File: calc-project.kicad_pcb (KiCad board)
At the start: 2 copper layers, 100 x 100 mm, 39 parts, among them J1 PinSocket_1x20_Right, J2 PinSocket_1x20_Left, J3 Conn_01x14, SW1 SW_Push_45deg, SW10 SW_Push_45deg, SW11 SW_Push_45deg, SW12 SW_Push_45deg, SW13 SW_Push_45deg, SW14 SW_Push_45deg, SW15 SW_Push_45deg, SW16 SW_Push_45deg, SW17 SW_Push_45deg, SW18 SW_Push_45deg, SW19 SW_Push_45deg, SW2 SW_Push_45deg, SW20 SW_Push_45deg, SW21 SW_Push_45deg, SW22 SW_Push_45deg, SW23 SW_Push_45deg, SW24 SW_Push_45deg, SW25 SW_Push_45deg, SW26 SW_Push_45deg, SW27 SW_Push_45deg, SW28 SW_Push_45deg, SW29 SW_Push_45deg, SW3 SW_Push_45deg, SW30 SW_Push_45deg, SW31 SW_Push_45deg, SW32 SW_Push_45deg, SW33 SW_Push_45deg, SW34 SW_Push_45deg, SW35 SW_Push_45deg, SW36 SW_Push_45deg, SW4 SW_Push_45deg, SW5 SW_Push_45deg, SW6 SW_Push_45deg, SW7 SW_Push_45deg, SW8 SW_Push_45deg, SW9 SW_Push_45deg

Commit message: random stuff, i think it helps
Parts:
- added H1: MountingHole, MountingHole:MountingHole_2.1mm, F.Cu at (35.0, 93.0)
- added H2: MountingHole, MountingHole:MountingHole_2.1mm, F.Cu at (124.0, 93.0)
- added H3: MountingHole, MountingHole:MountingHole_2.1mm, F.Cu at (35.0, 187.0)
- added H4: MountingHole, MountingHole:MountingHole_2.1mm, F.Cu at (124.0, 187.0)
- added H5: MountingHole, MountingHole:MountingHole_2.1mm, F.Cu at (49.0, 120.0)
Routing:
- net +3.3V: track 58.1 -> 60.8 mm
- net col 1: track 133.8 -> 131.4 mm
- net row 3: track 131.3 -> 129.7 mm
- net col 0: track 116.0 -> 114.4 mm
- net row 5: track 151.0 -> 149.9 mm
- net col 4: track 174.4 -> 174.7 mm, vias 2 -> 0

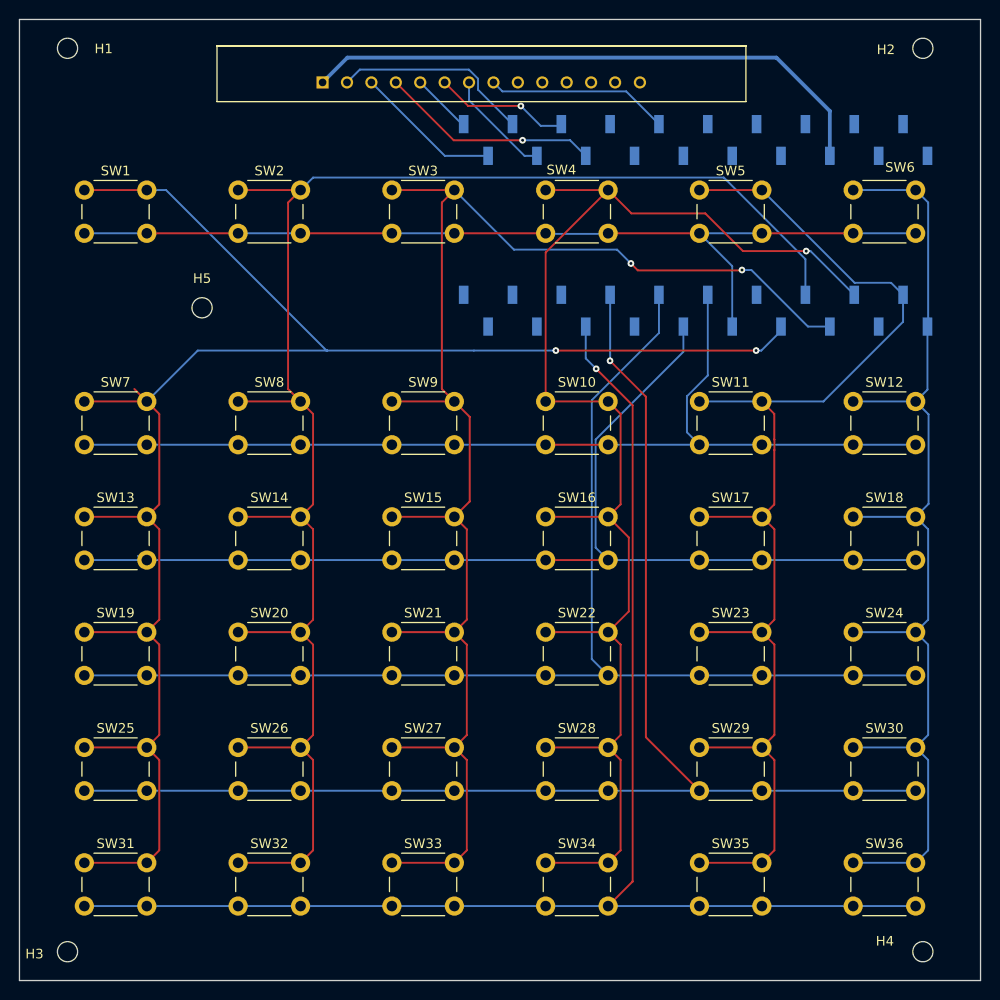
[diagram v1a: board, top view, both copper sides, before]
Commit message: better dimensions
Didn't have to be so wide, so I put all the components closer together and rerouted the whole thing
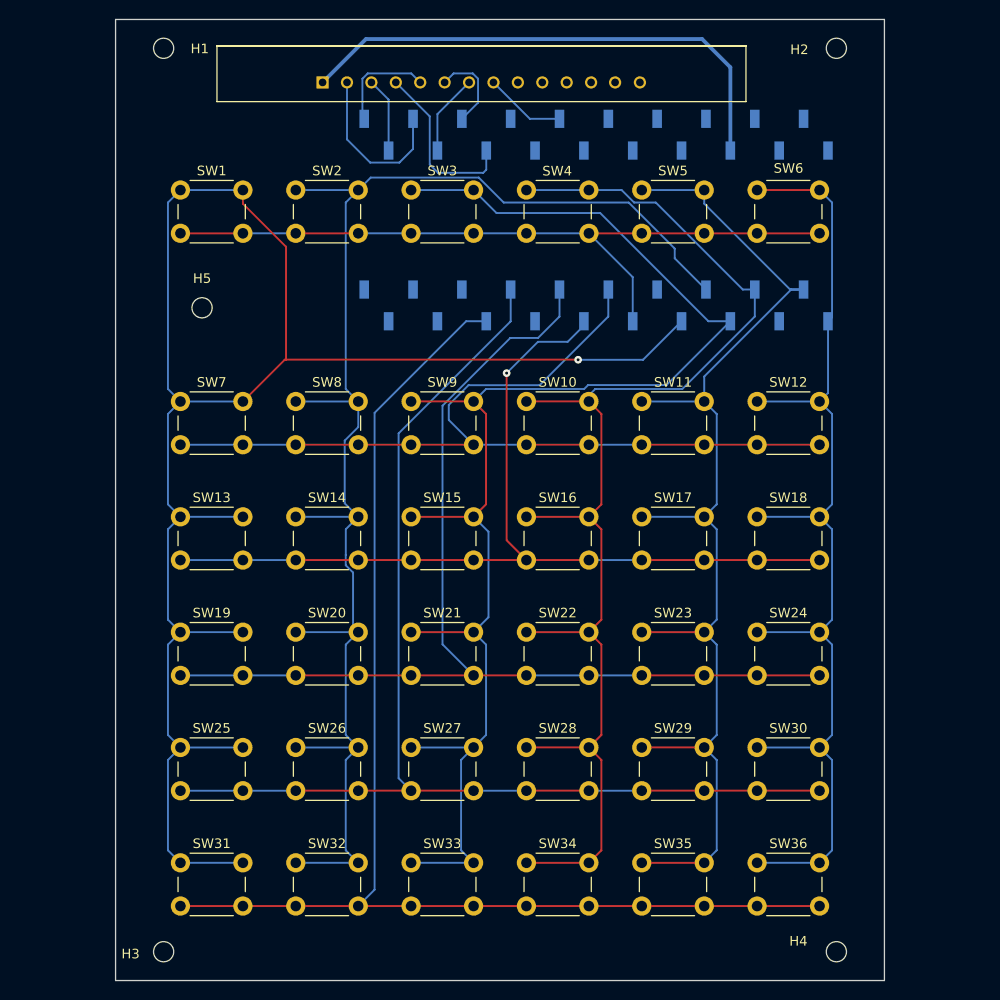
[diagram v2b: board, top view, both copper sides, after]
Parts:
- moved J1 10.4 mm to (90.0, 102.0)
- moved J2 10.4 mm to (90.0, 119.8)
- moved H1 10.0 mm to (45.0, 93.0)
- moved H3 10.0 mm to (45.0, 187.0)
- moved SW1 10.0 mm to (50.0, 110.0)
- moved SW12 10.0 mm to (110.0, 132.0)
- moved SW13 10.0 mm to (50.0, 144.0)
- moved SW18 10.0 mm to (110.0, 144.0)
- moved SW19 10.0 mm to (50.0, 156.0)
- moved SW24 10.0 mm to (110.0, 156.0)
- moved SW25 10.0 mm to (50.0, 168.0)
- moved SW30 10.0 mm to (110.0, 168.0)
- moved SW31 10.0 mm to (50.0, 180.0)
- moved SW36 10.0 mm to (110.0, 180.0)
- moved SW6 10.0 mm to (110.0, 110.0)
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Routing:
- net row 0: track 98.4 -> 77.5 mm
- net row 2: track 116.2 -> 97.3 mm, vias 0 -> 1
- net col 4: track 174.7 -> 156.6 mm
- net row 4: track 142.0 -> 124.0 mm, vias 1 -> 0
- net row 5: track 149.9 -> 134.1 mm, vias 1 -> 0
- net row 3: track 129.7 -> 114.7 mm
- net LED_CTRL: track 19.0 -> 8.44 mm
- net col 2: track 146.8 -> 137.0 mm, vias 1 -> 0
- net row 1: track 103.5 -> 94.9 mm
- net col 1: track 131.4 -> 123.5 mm
- net CS: track 15.3 -> 7.83 mm
- net +3.3V: track 60.8 -> 54.2 mm
- net col 3: track 160.0 -> 154.1 mm, vias 2 -> 0
- net col 5: track 188.3 -> 183.0 mm, vias 2 -> 1
- net SDI(MOSI): track 13.9 -> 8.96 mm, vias 1 -> 0
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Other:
- board size 100 x 100 mm -> 80 x 100 mm

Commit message: one last change
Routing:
- net +3.3V: track 54.2 -> 49.6 mm
- net RESET: track 18.4 -> 17.1 mm
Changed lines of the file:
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@@
-	)
-	(segment
-		(start 101.03 92.04)
-		(end 103.97 94.98)
-		(width 0.4)
-		(layer "B.Cu")
-		(net "+3.3V")
 	)
 	(segment
@@
 	)
 	(segment
-		(start 66.05 92.04)
-		(end 101.03 92.04)
+		(start 91.68 92.04)
+		(end 100.53 100.89)
 		(width 0.4)
 		(layer "B.Cu")
@@
 	)
 	(segment
-		(start 103.97 94.98)
+		(start 66.05 92.04)
+		(end 91.68 92.04)
+		(width 0.4)
+		(layer "B.Cu")
+		(net "+3.3V")
+	)
+	(segment
+		(start 100.53 100.89)
+		(end 100.53 101.69)
+		(width 0.4)
+		(layer "B.Cu")
+		(net "+3.3V")
+	)
+	(segment
+		(start 102.48 103.64)
 		(end 103.97 103.64)
+		(width 0.4)
+		(layer "B.Cu")
+		(net "+3.3V")
+	)
+	(segment
+		(start 100.53 101.69)
+		(end 102.48 103.64)
 		(width 0.4)
 		(layer "B.Cu")
@@
 	)
 	(segment
-		(start 78.25 105.96)
-		(end 78.57 105.64)
-		(width 0.2)
-		(layer "B.Cu")
-		(net "RESET")
-	)
-	(segment
-		(start 78.57 105.64)
+		(start 78.55 103.64)
 		(end 78.57 103.64)
 		(width 0.2)
@@
 	)
 	(segment
-		(start 72.69 105.09)
-		(end 73.56 105.96)
+		(start 69.16 96.55)
+		(end 72.69 100.08)
 		(width 0.2)
 		(layer "B.Cu")
@@
 	)
 	(segment
-		(start 73.56 105.96)
-		(end 78.25 105.96)
+		(start 73.45 105.85)
+		(end 76.34 105.85)
 		(width 0.2)
 		(layer "B.Cu")
@@
 	)
 	(segment
-		(start 69.16 96.55)
-		(end 72.69 100.08)
+		(start 72.69 105.09)
+		(end 73.45 105.85)
 		(width 0.2)
 		(layer "B.Cu")
+		(net "RESET")
+	)
+	(segment
+		(start 76.34 105.85)
+		(end 78.55 103.64)
+		(width 0.2)
+		(layer "B.Cu")

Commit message: created gerbers, added logo
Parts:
- added G***: LOGO, LOGO, F.Cu at (228.6, 101.6)
- added G***: LOGO, LOGO, F.Cu at (82.0, 120.0)
- added G***: LOGO, LOGO, F.Cu at (109.0, 120.0)
- added G***: LOGO, LOGO, F.Cu at (106.0, 120.0)
- added G***: LOGO, LOGO, F.Cu at (73.0, 120.0)
- added G***: LOGO, LOGO, F.Cu at (115.0, 120.0)
- added G***: LOGO, LOGO, F.Cu at (94.0, 120.0)
- added G***: LOGO, LOGO, F.Cu at (61.0, 120.0)
- added G***: LOGO, LOGO, F.Cu at (103.0, 120.0)
- added G***: LOGO, LOGO, F.Cu at (279.4, 101.6)
- added G***: LOGO, LOGO, F.Cu at (70.0, 120.0)
- added G***: LOGO, LOGO, F.Cu at (76.0, 120.0)
- added G***: LOGO, LOGO, F.Cu at (67.0, 120.0)
- added G***: LOGO, LOGO, F.Cu at (88.0, 120.0)
- added G***: LOGO, LOGO, F.Cu at (91.0, 120.0)
- added G***: LOGO, LOGO, F.Cu at (330.2, 101.6)
- added G***: LOGO, LOGO, F.Cu at (175.8, 101.6)
- added G***: LOGO, LOGO, F.Cu at (58.0, 120.0)
- added G***: LOGO, LOGO, F.Cu at (100.0, 120.0)
- added G***: LOGO, LOGO, F.Cu at (64.0, 120.0)
- added G***: LOGO, LOGO, F.Cu at (97.0, 120.0)
- added G***: LOGO, LOGO, F.Cu at (85.0, 120.0)
- added G***: LOGO, LOGO, F.Cu at (112.0, 120.0)
- added G***: LOGO, LOGO, F.Cu at (79.0, 120.0)
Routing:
- net row 2: track 97.3 -> 96.0 mm
- net row 4: track 124.0 -> 124.6 mm
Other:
- board text added: "@rod520"

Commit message: idek what just happened
but im trusting its fine
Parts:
- removed the G*** at (228.6, 101.6)
- removed the G*** at (279.4, 101.6)
- removed the G*** at (330.2, 101.6)
- removed the G*** at (175.8, 101.6)

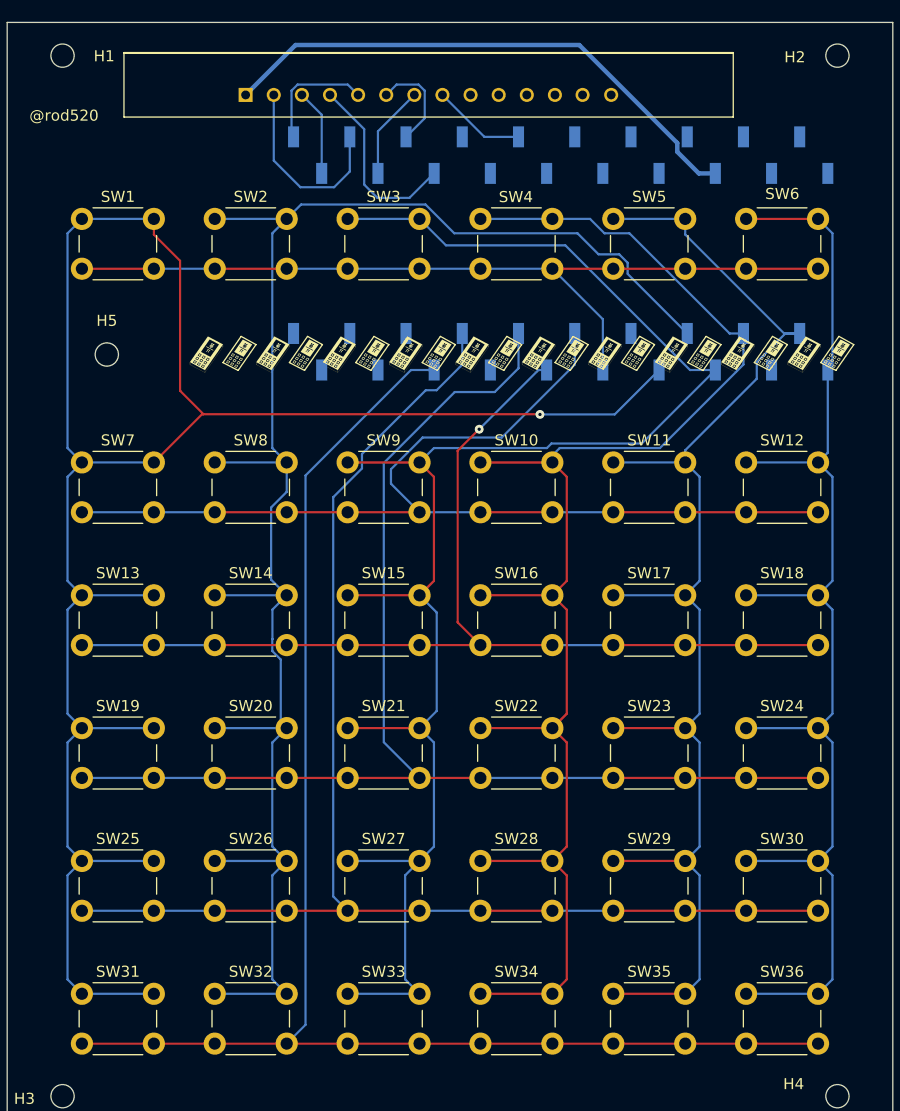
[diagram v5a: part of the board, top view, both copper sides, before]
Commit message: replaced old headers, now new ones
also took out routing for rows
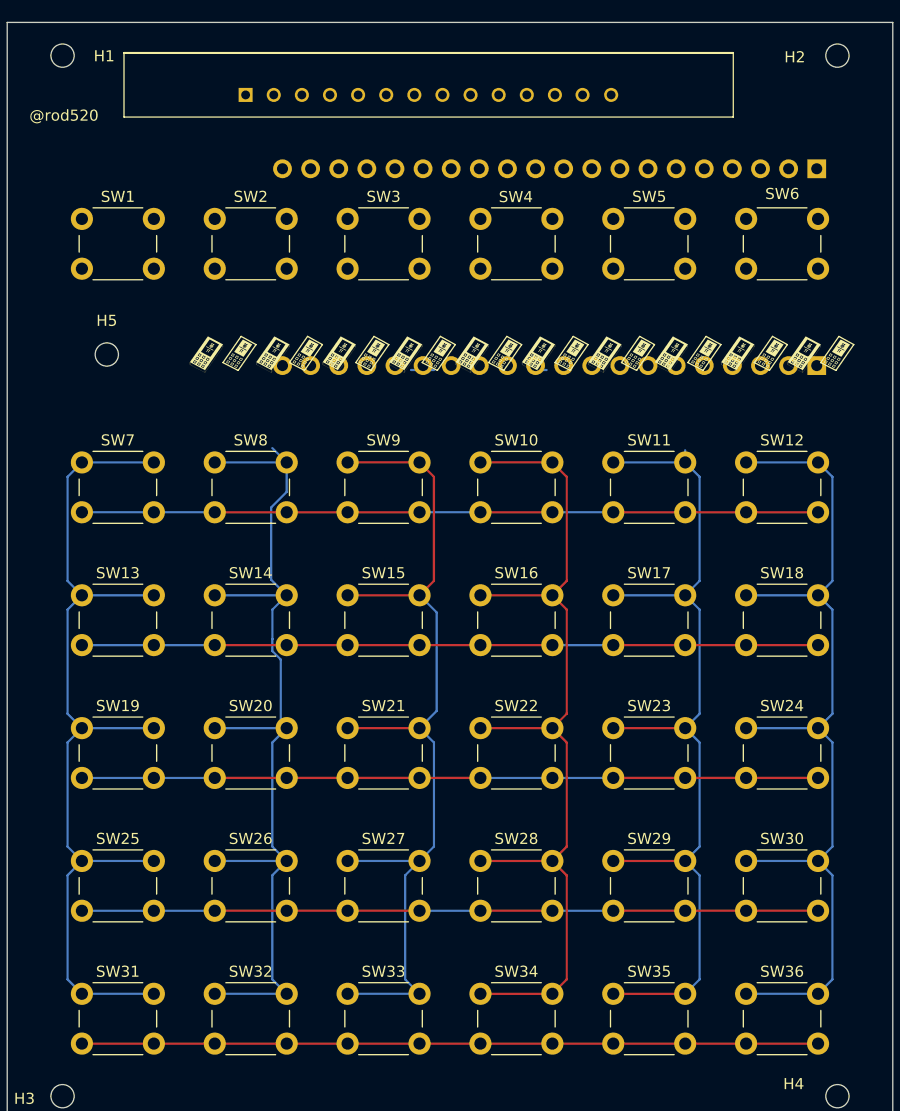
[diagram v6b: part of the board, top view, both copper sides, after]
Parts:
- J1, J2: footprint Connector_PinSocket_2.54mm:PinSocket_1x20_P2.54mm_Vertical_SMD_Pin1Left -> Connector_PinSocket_2.54mm:PinSocket_1x20_P2.54mm_Vertical
- moved J2 23.2 mm to (113.1, 121.0)
- moved J1 23.2 mm to (113.1, 103.2)
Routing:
- net col 5: track 183.0 -> 84.8 mm, vias 1 -> 0
- net row 0: track 77.5 -> 0.00 mm
- net col 4: track 156.6 -> 86.7 mm
- net col 3: track 154.1 -> 85.0 mm
- net row 5: track 134.1 -> 68.6 mm
- net row 4: track 124.6 -> 66.5 mm
- net col 2: track 137.0 -> 84.8 mm
- net +3.3V: track 49.6 -> 0.00 mm
- net row 3: track 115.1 -> 66.5 mm
- net col 1: track 123.5 -> 85.9 mm
- net col 0: track 114.4 -> 84.8 mm
- net row 2: track 96.0 -> 67.2 mm, vias 1 -> 0
- net row 1: track 94.8 -> 66.5 mm
- net GND: track 17.5 -> 0.00 mm
- net RESET: track 17.1 -> 0.00 mm
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
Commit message: routing
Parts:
- removed the G*** at (76.0, 120.0)
- removed the G*** at (109.0, 120.0)
- removed the G*** at (106.0, 120.0)
- removed the G*** at (73.0, 120.0)
- removed the G*** at (115.0, 120.0)
- removed the G*** at (94.0, 120.0)
- removed the G*** at (103.0, 120.0)
- removed the G*** at (70.0, 120.0)
- removed the G*** at (67.0, 120.0)
- removed the G*** at (88.0, 120.0)
- removed the G*** at (58.0, 120.0)
- removed the G*** at (91.0, 120.0)
- removed the G*** at (100.0, 120.0)
- removed the G*** at (64.0, 120.0)
- removed the G*** at (97.0, 120.0)
- removed the G*** at (85.0, 120.0)
- removed the G*** at (112.0, 120.0)
- removed the G*** at (79.0, 120.0)
- removed the G*** at (82.0, 120.0)
- added G***: LOGO, LOGO, F.Cu at (59.6, 121.2)
- G***: moved to B.Cu
- moved G*** 58.0 mm to (114.8, 98.4), turned to 180 degrees
- moved J1 46.3 mm to (66.8, 102.2), turned to -90 degrees
- moved J2 2.18 mm to (115.1, 120.0)
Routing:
- net col 4: track 86.7 -> 174.7 mm
- net col 5: track 84.8 -> 162.3 mm
- net col 3: track 85.0 -> 156.2 mm
- net row 0: track 0.00 -> 68.8 mm
- net row 5: track 68.6 -> 129.7 mm
- net col 2: track 84.8 -> 138.8 mm
- net row 4: track 66.5 -> 117.7 mm
- net +3.3V: track 0.00 -> 46.8 mm
- net row 3: track 66.5 -> 106.6 mm
- net col 1: track 85.9 -> 123.5 mm
- net col 0: track 84.8 -> 114.8 mm
- net row 2: track 67.2 -> 94.9 mm
- net row 1: track 66.5 -> 81.8 mm
- net RESET: track 0.00 -> 14.8 mm
- net GND: track 0.00 -> 11.9 mm
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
